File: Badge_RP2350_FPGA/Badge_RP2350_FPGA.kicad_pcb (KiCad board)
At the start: 2 copper layers, 100 x 150 mm, 110 parts, among them J1 USB_C_Receptacle_USB2.0_16P, J2 Conn_01x03_Pin, J3 Conn_01x15_Pin, J4 Conn_01x15_Pin, SW1 SW_Push, SW12 On/Off, SW2 SW_Push, U1 RP2350_60QFN, U2 GW1N-LV9QN88C6_I5_, U3 ME6211C12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

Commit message: edit schematics visually and edit pcb
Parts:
- U3: footprint semitovpartslibrary:ME6211C12 -> semitovpartslibrary:SOT-23-5_L3.0-W1.7-P0.95-LS2.8-BL
- U4: footprint semitovpartslibrary:TMI7003C -> semitovpartslibrary:QFN-20_L3.0-W3.0-P0.40-BL-EP1.7
- moved J1 47.8 mm to (146.0, 182.0), turned to 90 degrees
- moved U1 42.3 mm to (138.0, 165.4)
- moved R18 38.9 mm to (137.0, 192.5)
- moved R20 38.9 mm to (140.0, 192.5)
- moved U3 34.9 mm to (145.2, 190.8), turned to 90 degrees
- moved L2 33.6 mm to (117.0, 179.0)
- moved R8 32.1 mm to (137.0, 171.5), turned to 90 degrees
- moved R7 27.7 mm to (138.0, 171.5), turned to 90 degrees
- moved U4 25.3 mm to (136.1, 180.2)
- moved C46 18.6 mm to (133.5, 198.0)
- moved C45 13.9 mm to (136.5, 187.0)
- moved C47 12.8 mm to (132.5, 185.0)
- moved C1 10.5 mm to (131.5, 194.0)
- moved C5 10.3 mm to (68.0, 186.0)
- moved C48 8.12 mm to (139.5, 179.0), turned to 90 degrees
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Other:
- board text added: "PCB designed by: Tan S. Akıncı Valerio Donnini Alessandro Bocchino Carlo Bendelli Arianna Bruno"
- board text removed: "PCB designed by: Tan S. Akıncı Valerio Donnini Alessandro Bochino Carlo Bendelli Arianna Bruno"

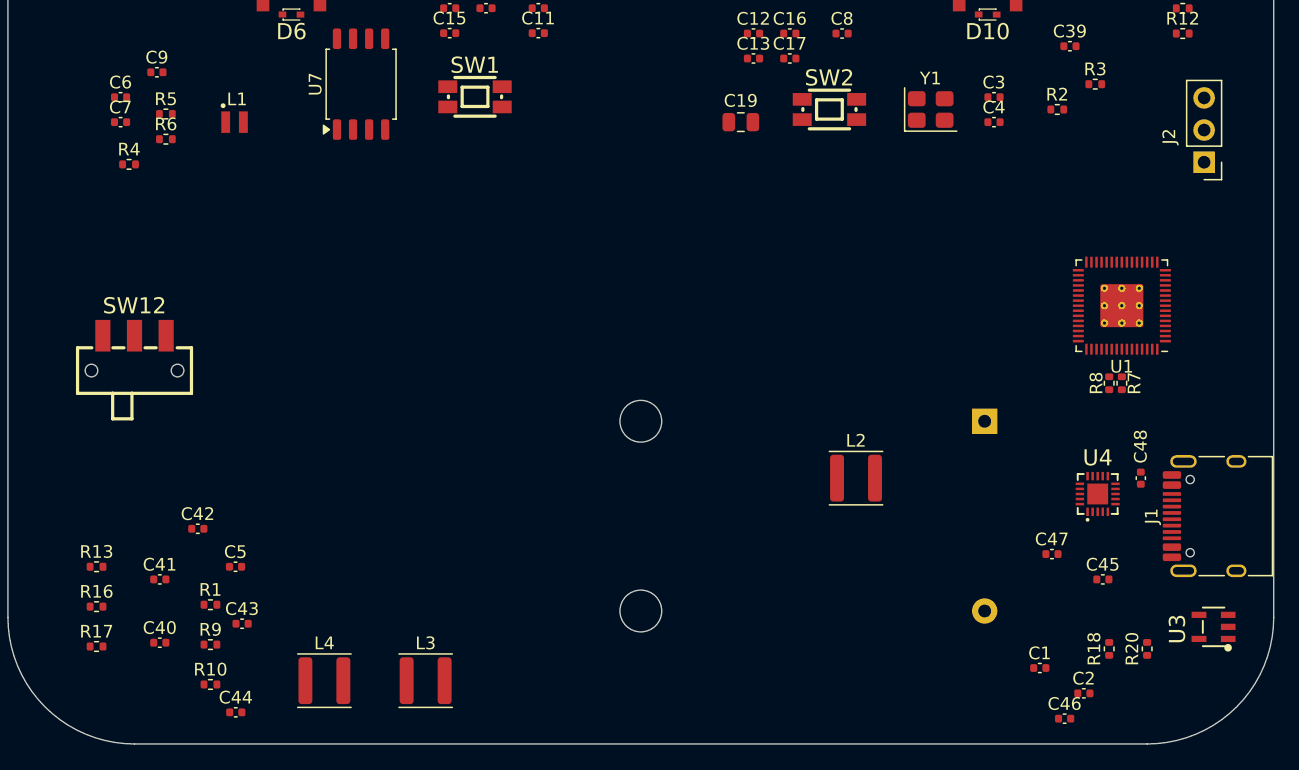
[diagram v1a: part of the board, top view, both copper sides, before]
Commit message: edit pcb placement slightly
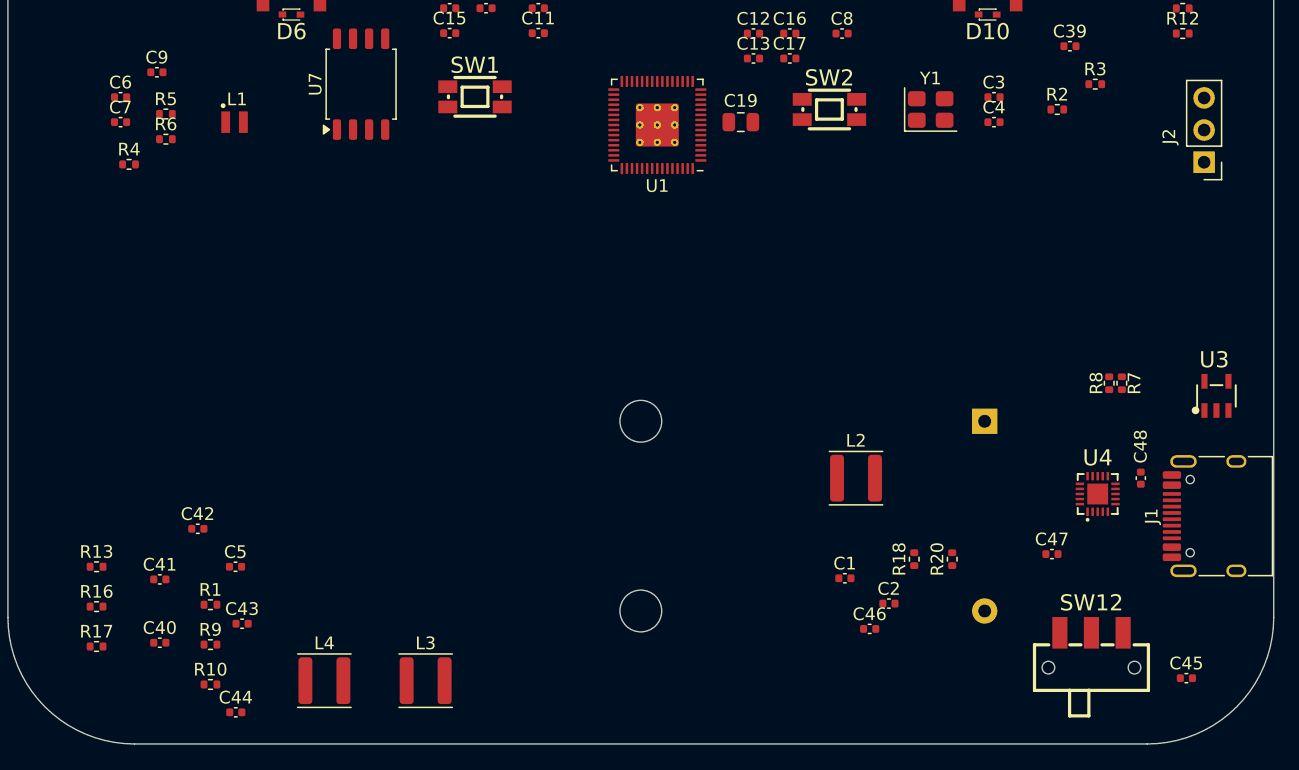
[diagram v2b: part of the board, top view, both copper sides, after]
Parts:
- moved SW12 79.2 mm to (135.6, 191.2)
- moved U1 39.4 mm to (101.3, 151.1)
- moved U3 18.2 mm to (145.5, 172.5), turned to 0 degrees
- moved C1 17.0 mm to (116.1, 186.9)
- moved C2 17.0 mm to (119.6, 188.9)
- moved R18 17.0 mm to (121.6, 185.4)
- moved R20 17.0 mm to (124.6, 185.4)
- moved C46 17.0 mm to (118.1, 190.9)
- moved C45 10.2 mm to (143.1, 194.8)

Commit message: power placement
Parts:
- moved C40 67.5 mm to (128.8, 182.0), turned to -90 degrees
- moved R9 62.3 mm to (127.5, 182.0), turned to 90 degrees
- moved R10 61.9 mm to (126.5, 182.0), turned to 90 degrees
- moved R16 58.6 mm to (112.2, 169.5)
- moved C43 57.5 mm to (125.3, 182.0), turned to 90 degrees
- moved R13 55.9 mm to (112.2, 194.8), turned to 180 degrees
- moved R17 55.4 mm to (112.2, 196.0), turned to 180 degrees
- moved C41 51.3 mm to (112.2, 197.2), turned to 180 degrees
- moved R1 49.7 mm to (112.2, 170.8), turned to 180 degrees
- moved C42 49.7 mm to (112.2, 167.8)
- moved C5 46.4 mm to (112.3, 172.3), turned to 180 degrees
- moved C44 44.4 mm to (112.2, 193.5), turned to 180 degrees
- moved L4 42.5 mm to (112.8, 175.8), turned to -90 degrees
- moved L3 41.1 mm to (122.0, 182.0), turned to 180 degrees
- moved R8 39.5 mm to (100.1, 157.4)
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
